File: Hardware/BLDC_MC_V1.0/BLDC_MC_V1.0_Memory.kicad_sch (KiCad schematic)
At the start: 9 parts, among them U8 25LC256-E_SN

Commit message: Update recovery files of the project
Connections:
- net SCK: now also R44.2, U8.6 (SCK)
- net NWP: now reaches R17.1, U8.3 (~WP)
- net SI: now reaches R21.2, U8.5 (SI)
- net NHOLD: now reaches R18.1, U8.7 (~HOLD)
- net CS: now reaches R16.1, R19.1, U8.1 (~CS)
- net SO: now reaches R20.2, U8.2 (SO)
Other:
- moved on the sheet: R20, R21, R44
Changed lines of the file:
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@@
 	)
 	(rectangle
-		(start 180.34 83.82)
-		(end 198.12 95.25)
+		(start 185.42 83.82)
+		(end 203.2 95.25)
 		(stroke
 			(width 0)
@@
 	)
 	(rectangle
-		(start 180.34 95.25)
-		(end 198.12 109.22)
+		(start 185.42 95.25)
+		(end 203.2 109.22)
 		(stroke
 			(width 0)
@@
 	(rectangle
 		(start 80.01 69.85)
-		(end 208.28 124.46)
+		(end 213.36 124.46)
 		(stroke
 			(width 0)
@@
 	(text "Placed 3-5mm\nfrom EEPROM\n"
 		(exclude_from_sim no)
-		(at 189.23 87.63 0)
+		(at 194.31 87.63 0)
 		(effects
 			(font
@@
 	(text "Placed 3-5mm \nfrom MCU"
 		(exclude_from_sim no)
-		(at 189.23 106.68 0)
+		(at 194.31 106.68 0)
 		(effects
 			(font
@@
 	(wire
 		(pts
-			(xy 180.34 102.87) (xy 185.42 102.87)
-		)
-		(stroke
-			(width 0)
-			(type default)
-		)
-	)
-	(wire
-		(pts
 			(xy 144.78 81.28) (xy 144.78 83.82)
 		)
@@
 	(wire
 		(pts
-			(xy 193.04 102.87) (xy 199.39 102.87)
-		)
-		(stroke
-			(width 0)
-			(type default)
-		)
-	)
-	(wire
-		(pts
-			(xy 180.34 97.79) (xy 185.42 97.79)
+			(xy 198.12 102.87) (xy 204.47 102.87)
 		)
 		(stroke
@@
 	(wire
 		(pts
-			(xy 180.34 92.71) (xy 185.42 92.71)
-		)
-		(stroke
-			(width 0)
-			(type default)
-		)
-	)
-	(wire
-		(pts
-			(xy 193.04 97.79) (xy 199.39 97.79)
+			(xy 198.12 97.79) (xy 204.47 97.79)
 		)
 		(stroke
@@
 	(wire
 		(pts
+			(xy 180.34 102.87) (xy 190.5 102.87)
+		)
+		(stroke
+			(width 0)
+			(type default)
+		)
+	)
+	(wire
+		(pts
+			(xy 180.34 92.71) (xy 190.5 92.71)
+		)
+		(stroke
+			(width 0)
+			(type default)
+		)
+	)
+	(wire
+		(pts
 			(xy 140.97 83.82) (xy 140.97 86.36)
 		)
@@
 	(wire
 		(pts
+			(xy 180.34 97.79) (xy 190.5 97.79)
+		)
+		(stroke
+			(width 0)
+			(type default)
+		)
+	)
+	(wire
+		(pts
 			(xy 128.27 86.36) (xy 128.27 83.82)
 		)
@@
 	(wire
 		(pts
-			(xy 193.04 92.71) (xy 199.39 92.71)
+			(xy 198.12 92.71) (xy 204.47 92.71)
 		)
 		(stroke
@@
 			(width 0)
 			(type default)
+		)
+	)
+	(label "SI"
+		(at 181.61 97.79 0)
+		(effects
+			(font
+				(size 1.27 1.27)
+			)
+			(justify left bottom)
+		)
+	)
+	(label "NHOLD"
+		(at 135.89 97.79 0)
+		(effects
+			(font
+				(size 1.27 1.27)
+			)
+			(justify left bottom)
+		)
+	)
+	(label "SCK"
+		(at 181.61 102.87 0)
+		(effects
+			(font
+				(size 1.27 1.27)
+			)
+			(justify left bottom)
+		)
+	)
+	(label "SO"
+		(at 181.61 92.71 0)
+		(effects
+			(font
+				(size 1.27 1.27)
+			)
+			(justify left bottom)
+		)
+	)
+	(label "CS"
+		(at 142.24 95.25 0)
+		(effects
+			(font
+				(size 1.27 1.27)
+			)
+			(justify left bottom)
+		)
+	)
+	(label "NWP"
+		(at 135.89 100.33 0)
+		(effects
+			(font
+				(size 1.27 1.27)
+			)
+			(justify left bottom)
 		)
 	)
 	(hierarchical_label "SCK"
 		(shape input)
-		(at 199.39 102.87 0)
+		(at 204.47 102.87 0)
 		(effects
 			(font
@@
 	(hierarchical_label "MOSI"
 		(shape input)
-		(at 199.39 97.79 0)
+		(at 204.47 97.79 0)
 		(effects
 			(font
@@
 	(hierarchical_label "MISO"
 		(shape output)
-		(at 199.39 92.71 0)
+		(at 204.47 92.71 0)
 		(effects
 			(font
@@
 	(symbol
 		(lib_id "Device:R")
-		(at 189.23 102.87 270)
+		(at 194.31 102.87 270)
 		(unit 1)
 		(body_style 1)
@@
 		(dnp no)
 		(property "Reference" "R44"
-			(at 184.15 101.6 90)
+			(at 189.23 101.6 90)
 			(show_name no)
 			(do_not_autoplace no)
@@
 		)
 		(property "Value" "33R"
-			(at 194.31 101.6 90)
+			(at 199.39 101.6 90)
 			(show_name no)
 			(do_not_autoplace no)
@@
 		)
 		(property "Footprint" "Resistor_SMD:R_0603_1608Metric"
-			(at 189.23 101.092 90)
+			(at 194.31 101.092 90)
 			(hide yes)
 			(show_name no)
@@
 		)
 		(property "Datasheet" ""
-			(at 189.23 102.87 0)
+			(at 194.31 102.87 0)
 			(hide yes)
 			(show_name no)
@@
 		)
 		(property "Description" "Resistor"
-			(at 189.23 102.87 0)
+			(at 194.31 102.87 0)
 			(hide yes)
 			(show_name no)
@@
 		)
 		(property "LCSC_PN" "C108661"
-			(at 189.23 102.87 0)
+			(at 194.31 102.87 0)
 			(hide yes)
 			(show_name no)
@@
 		)
 		(property "MP" "RC0603FR-0733RL"
-			(at 189.23 102.87 0)
+			(at 194.31 102.87 0)
 			(hide yes)
 			(show_name no)
@@
 		)
 		(property "Assembled" "Yes"
-			(at 189.23 102.87 0)
+			(at 194.31 102.87 0)
 			(hide yes)
 			(show_name no)
@@
 	(symbol
 		(lib_id "Device:R")
-		(at 189.23 97.79 270)
+		(at 194.31 97.79 270)
 		(unit 1)
 		(body_style 1)
@@
 		(dnp no)
 		(property "Reference" "R21"
-			(at 184.15 96.52 90)
+			(at 189.23 96.52 90)
 			(show_name no)
 			(do_not_autoplace no)
@@
 		)
 		(property "Value" "33R"
-			(at 194.31 96.52 90)
+			(at 199.39 96.52 90)
 			(show_name no)
 			(do_not_autoplace no)
@@
 		)
 		(property "Footprint" "Resistor_SMD:R_0603_1608Metric"
-			(at 189.23 96.012 90)
+			(at 194.31 96.012 90)
 			(hide yes)
 			(show_name no)
@@
 		)
 		(property "Datasheet" ""
-			(at 189.23 97.79 0)
+			(at 194.31 97.79 0)
 			(hide yes)
 			(show_name no)
@@
 		)
 		(property "Description" "Resistor"
-			(at 189.23 97.79 0)
+			(at 194.31 97.79 0)
 			(hide yes)
 			(show_name no)
@@
 		)
 		(property "LCSC_PN" "C108661"
-			(at 189.23 97.79 0)
+			(at 194.31 97.79 0)
 			(hide yes)
 			(show_name no)
@@
 		)
 		(property "MP" "RC0603FR-0733RL"
-			(at 189.23 97.79 0)
+			(at 194.31 97.79 0)
 			(hide yes)
 			(show_name no)
@@
 		)
 		(property "Assembled" "Yes"
-			(at 189.23 97.79 0)
+			(at 194.31 97.79 0)
 			(hide yes)
 			(show_name no)
@@
 	(symbol
 		(lib_id "Device:R")
-		(at 189.23 92.71 270)
+		(at 194.31 92.71 270)
 		(unit 1)
 		(body_style 1)
@@
 		(dnp no)
 		(property "Reference" "R20"
-			(at 184.15 91.44 90)
+			(at 189.23 91.44 90)
 			(show_name no)
 			(do_not_autoplace no)
@@
 		)
 		(property "Value" "33R"
-			(at 194.31 91.44 90)
+			(at 199.39 91.44 90)
 			(show_name no)
 			(do_not_autoplace no)
@@
 		)
 		(property "Footprint" "Resistor_SMD:R_0603_1608Metric"
-			(at 189.23 90.932 90)
+			(at 194.31 90.932 90)
 			(hide yes)
 			(show_name no)
@@
 		)
 		(property "Datasheet" ""
-			(at 189.23 92.71 0)
+			(at 194.31 92.71 0)
 			(hide yes)
 			(show_name no)
@@
 		)
 		(property "Description" "Resistor"
-			(at 189.23 92.71 0)
+			(at 194.31 92.71 0)
 			(hide yes)
 			(show_name no)
@@
 		)
 		(property "LCSC_PN" "C108661"
-			(at 189.23 92.71 0)
+			(at 194.31 92.71 0)
 			(hide yes)
 			(show_name no)
@@
 		)
 		(property "MP" "RC0603FR-0733RL"
-			(at 189.23 92.71 0)
+			(at 194.31 92.71 0)
 			(hide yes)
 			(show_name no)
@@
 		)
 		(property "Assembled" "Yes"
-			(at 189.23 92.71 0)
-			(hide yes)
-			(show_name no)
+			(at 194.31 92.71 0)
+			(hide yes)
+			(show_name no)

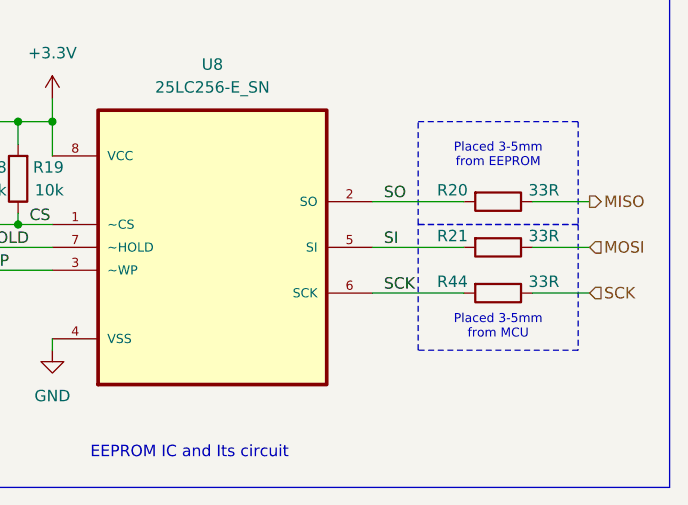
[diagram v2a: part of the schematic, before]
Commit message: Update the plaacement of PCB
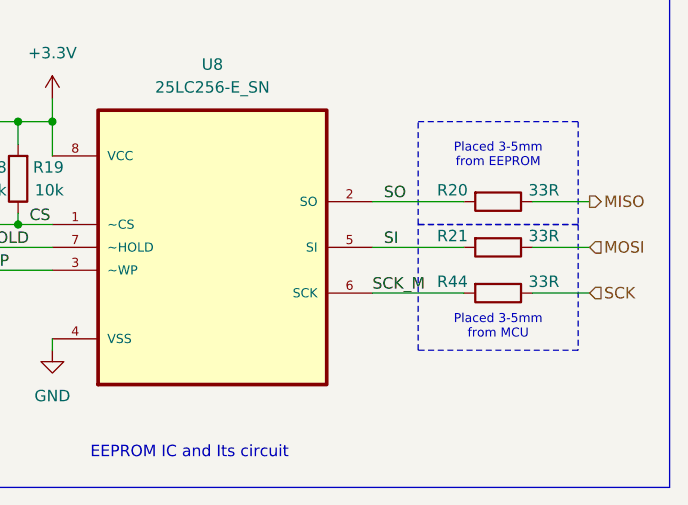
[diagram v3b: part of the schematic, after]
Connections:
- net SCK: no longer R44.2, U8.6 (SCK)
- new net SCK_M: R44.2, U8.6 (SCK)
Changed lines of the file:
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@@
 		)
 	)
-	(label "SCK"
-		(at 181.61 102.87 0)
+	(label "SCK_M"
+		(at 180.34 102.87 0)
 		(effects
 			(font
